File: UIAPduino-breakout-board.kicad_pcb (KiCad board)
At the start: 2 copper layers, 56.6 x 54.1 mm, 14 parts, among them J1 Conn_01x20_Pin, J2 Conn_01x20_Socket, J3 Barrel_Jack_Switch, SW1 SW_SPDT_312, SW2 SW_SPDT_312, SW3 SW_Slide_DPDT, U3 L7805

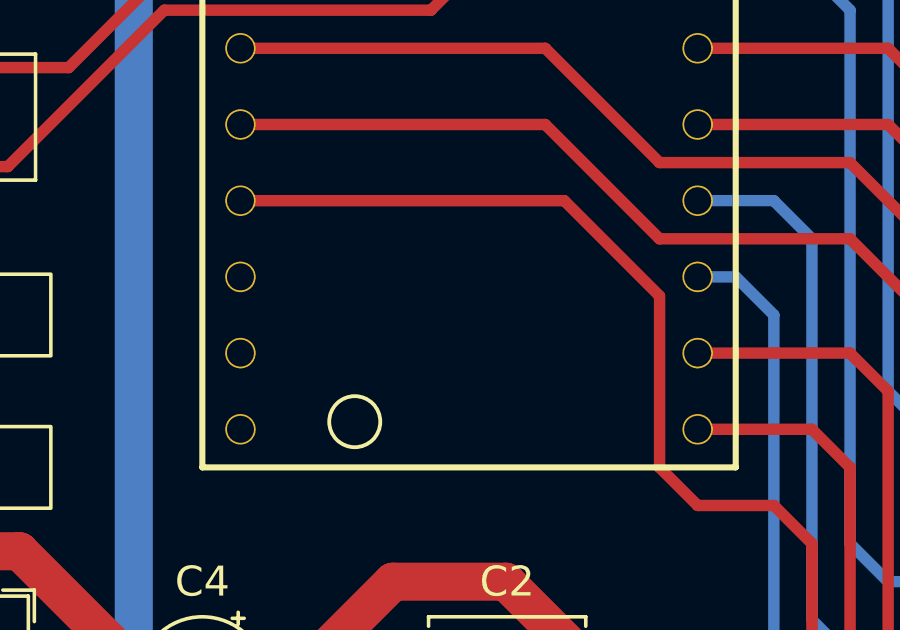
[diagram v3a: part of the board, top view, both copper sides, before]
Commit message: なくしてた接続を戻した
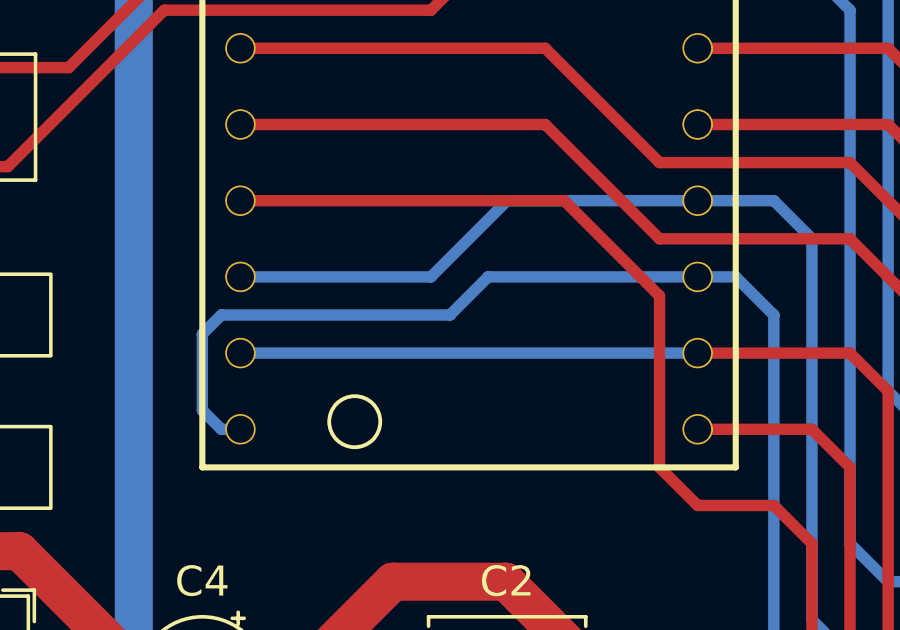
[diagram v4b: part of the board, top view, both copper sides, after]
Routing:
- net Net-(J1-Pin_17): track 37.9 -> 59.3 mm
- net Net-(J1-Pin_15): track 35.3 -> 51.6 mm
- net Net-(J1-Pin_16): track 32.8 -> 48.0 mm
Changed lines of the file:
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@@
+	(segment
+		(start 160.02 87.63)
+		(end 153.67 87.63)
+		(width 0.381)
+		(layer "B.Cu")
+		(net 4)
+	)
+	(segment
+		(start 153.67 87.63)
+		(end 151.13 90.17)
+		(width 0.381)
+		(layer "B.Cu")
+		(net 4)
+	)
 	(segment
 		(start 160.02 87.63)
@@
 	)
 	(segment
+		(start 151.13 90.17)
+		(end 144.78 90.17)
+		(width 0.381)
+		(layer "B.Cu")
+		(net 4)
+	)
+	(segment
 		(start 165.1 102.87)
 		(end 163.83 101.6)
@@
 	)
 	(segment
+		(start 151.765 91.44)
+		(end 144.145 91.44)
+		(width 0.381)
+		(layer "B.Cu")
+		(net 12)
+	)
+	(segment
 		(start 163.83 107.95)
 		(end 162.56 106.68)
@@
 	(segment
 		(start 160.02 90.17)
+		(end 153.035 90.17)
+		(width 0.381)
+		(layer "B.Cu")
+		(net 12)
+	)
+	(segment
+		(start 160.02 90.17)
 		(end 161.29 90.17)
+		(width 0.381)
+		(layer "B.Cu")
+		(net 12)
+	)
+	(segment
+		(start 144.145 95.25)
+		(end 144.78 95.25)
+		(width 0.381)
+		(layer "B.Cu")
+		(net 12)
+	)
+	(segment
+		(start 144.145 91.44)
+		(end 143.51 92.075)
 		(width 0.381)
 		(layer "B.Cu")
@@
 	)
 	(segment
+		(start 143.51 94.615)
+		(end 144.145 95.25)
+		(width 0.381)
+		(layer "B.Cu")
+		(net 12)
+	)
+	(segment
 		(start 162.56 106.68)
 		(end 162.56 91.44)
@@
 	)
 	(segment
+		(start 143.51 92.075)
+		(end 143.51 94.615)
+		(width 0.381)
+		(layer "B.Cu")
+		(net 12)
+	)
+	(segment
+		(start 153.035 90.17)
+		(end 151.765 91.44)
+		(width 0.381)
+		(layer "B.Cu")
+		(net 12)
+	)
+	(segment
 		(start 171.45 110.49)
 		(end 166.37 110.49)
@@
 		(width 0.381)
 		(layer "B.Cu")
+		(net 14)
+	)
+	(segment
+		(start 160.02 92.71)
+		(end 144.78 92.71)
+		(width 0.381)
+		(layer "B.Cu")
